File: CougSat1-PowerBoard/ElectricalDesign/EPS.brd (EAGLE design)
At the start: 90.4 x 95.8 mm, 428 parts, among them J1 Deployable 0, J10 Battery -, J11 PGND, J12 Battery +, J13 VBatt, J2 PV0, J3 PV1, J4 Umbilical, J5 CougSat Card, J6 SWD, J7 PV2, J8 PV3, J9 Deployable 1, Q1 CSD25402Q3A, Q10 CSD25402Q3A, Q11 DMN53D0LDW, Q12 CSD25402Q3A, Q13 DMN53D0LDW, Q14 CSD25402Q3A, Q15 DMN53D0LDW, Q16 CSD25402Q3A, Q17 CSD25402Q3A, Q18 CSD25402Q3A, Q19 DMN53D0LDW, Q2 DMN2008LFU, Q20 CSD25402Q3A, Q21 CSD25402Q3A, Q22 CSD25402Q3A, Q23 DMN53D0LDW, Q24 CSD25402Q3A, Q25 DMN53D0LDW, Q26 CSD25402Q3A, Q27 DMN53D0LDW, Q28 CSD25402Q3A, Q29 CSD25402Q3A, Q3 DMN2008LFU, Q30 CSD25402Q3A, Q31 DMN53D0LDW, Q32 CSD25402Q3A, Q33 DMN53D0LDW, Q34 CSD25402Q3A, Q35 CSD25402Q3A, Q36 DMN53D0LDW, Q37 CSD25402Q3A, Q38 CSD25402Q3A, Q39 DMN53D0LDW, Q4 CSD25402Q3A, Q40 CSD25402Q3A, Q41 CSD25402Q3A, Q42 DMN53D0LDW, Q43 CSD25402Q3A, Q5 DMN53D0LDW, Q6 DMN53D0LDW, Q7 CSD25402Q3A, Q8 CSD25402Q3A, Q9 CSD25402Q3A, SW1 ESE24MH1, U1 INA199C2, U10 INA199C2, U11 INA199C1, U12 AD7689, U13 INA199C2, U14 INA199C2, U15 TXS0102DQM, U16 TXS0102DQM, U17 AD8515, U18 BQ29700, U19 INA199C2, U2 AD7689, U20 TXS0102DQM, U21 TXS0102DQM, U22 STM32L476RGT, U23 AD7291, U24 INA199C2, U25 INA199C2, U26 BQ29700, U27 INA199C2, U28 INA199C2, U29 INA199C2, U3 AD8515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

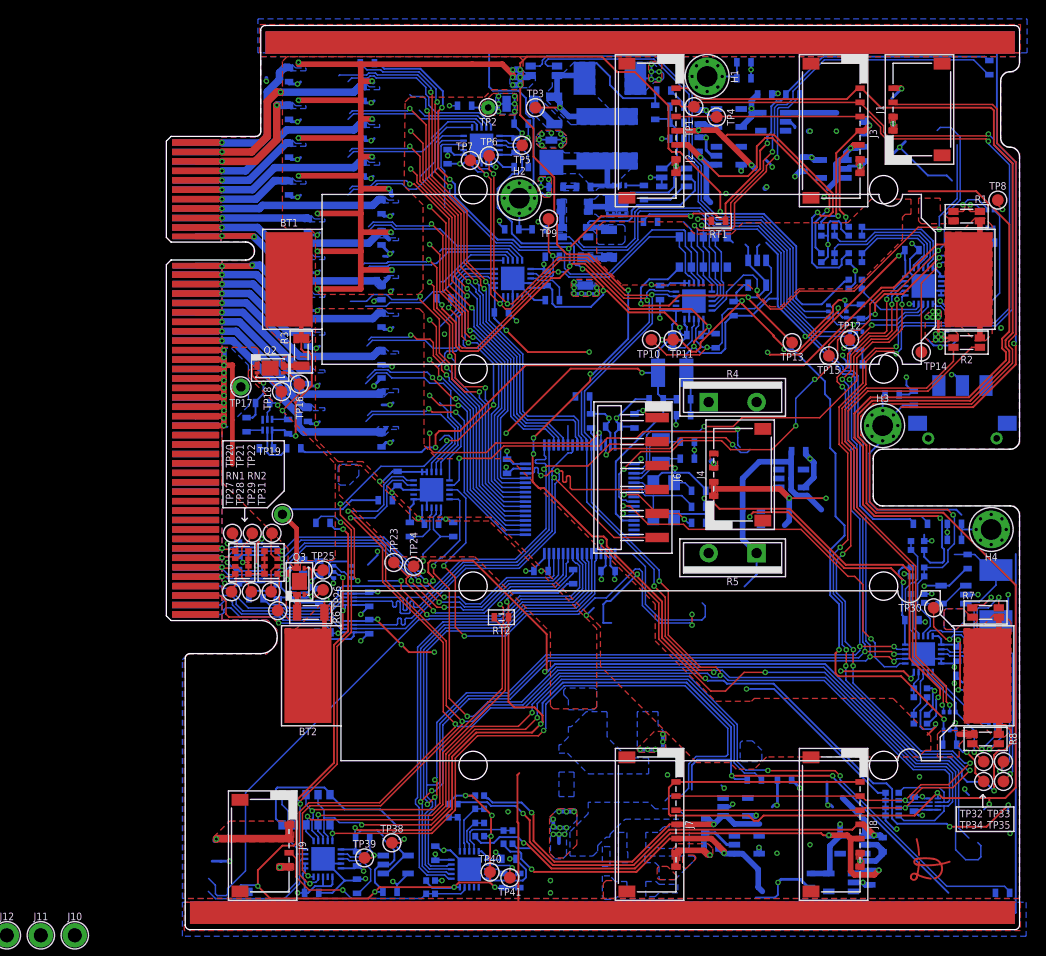
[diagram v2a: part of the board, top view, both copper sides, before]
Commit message: Removed unhelpful copper
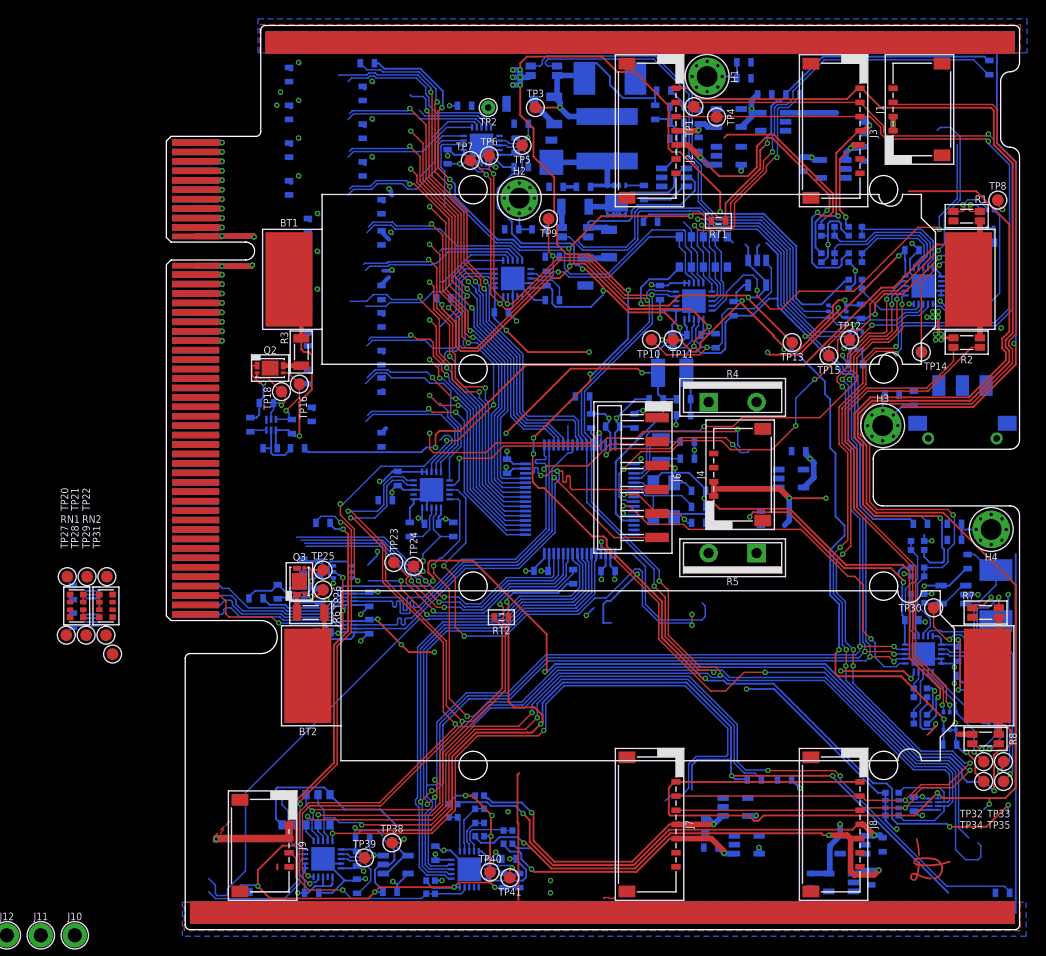
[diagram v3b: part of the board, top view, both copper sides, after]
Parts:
- removed TP17, TP19: TEST_POINT-THT-1.0, CougsInSpace-Connectors:THT-1.0
- moved C51 18.1 mm to (-9.90, -15.1)
- moved C54 18.1 mm to (-9.90, -12.2)
- moved RN1 18.1 mm to (-9.50, -13.6)
- moved RN2 18.1 mm to (-6.40, -13.6)
- moved TP20 18.1 mm to (-10.5, -10.5)
- moved TP21 18.1 mm to (-8.40, -10.5)
- moved TP22 18.1 mm to (-6.30, -10.5)
- moved TP27 18.1 mm to (-10.6, -16.7)
- moved TP28 18.1 mm to (-8.50, -16.7)
- moved TP29 18.1 mm to (-6.40, -16.7)
- moved TP31 18.1 mm to (-5.70, -18.7)
- moved U20 18.1 mm to (-7.80, -15.1)
- moved U21 18.1 mm to (-7.80, -12.2)
- moved C68 0.40 mm to (11.0, 3.10)
- moved C74 0.40 mm to (15.4, 6.70)
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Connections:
- net BATTERY-: no longer TP17.1, TP19.1
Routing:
- net PGND: track 826.7 -> 0.00 mm, vias 122 -> 0
- net 3.3V: track 713.2 -> 592.5 mm, vias 57 -> 55
- net PR_3.3V-0: track 74.9 -> 5.92 mm, vias 3 -> 1
- net CHASSIS: track 252.5 -> 217.8 mm
- net PR_BATT-6: track 28.5 -> 6.27 mm
- net PR_BATT-4: track 26.5 -> 5.85 mm
- net PR_3.3V-1: track 25.9 -> 5.92 mm
- net PR_BATT-2: track 25.4 -> 5.92 mm
- net DGND: track 466.0 -> 447.2 mm, vias 26 -> 24
- net PR_BATT-0: track 24.6 -> 5.92 mm
- net PR_3.3V-9: track 25.0 -> 6.86 mm
- net CHASSIS_RBF1: track 36.2 -> 18.8 mm
- net PR_3.3V-7: track 23.2 -> 5.92 mm
- net PR_3.3V-3: track 22.9 -> 5.92 mm
- net PR_3.3V-5: track 22.0 -> 5.92 mm
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- removed copper zone on layer 1, net 3.3V
- removed copper zone on layer 15, net 3.3V
- removed copper zone on layer 16, net 3.3V
- removed copper zone on layer 2, net 3.3V
- removed copper zone on layer 1, net 3.3V-B
- removed copper zone on layer 15, net 3.3V-B
- removed copper zone on layer 16, net 3.3V-B
- removed copper zone on layer 2, net 3.3V-B
- removed copper zone on layer 16, net 3.3V_I
- removed copper zone on layer 16, net 3.3V_I-B
- removed copper zone on layer 16, net 3.3V_ISENS
- removed copper zone on layer 16, net 3.3V_ISENS-B
- removed copper zone on layer 16, net 3.3V_REG_BUCK_NODE
- removed copper zone on layer 16, net 3.3V_REG_BUCK_NODE-B
- removed copper zone on layer 16, net 3.3V_REG_INCAP
- removed copper zone on layer 16, net 3.3V_REG_INCAP-B
- removed copper zone on layer 16, net 3.3V_REG_OUTCAP
- removed copper zone on layer 16, net 3.3V_REG_OUTCAP-B
- removed copper zone on layer 16, net 3.3V_REG_RSENS
- removed copper zone on layer 16, net 3.3V_REG_RSENS-B
- removed copper zone on layer 16, net 3.3V_REG_SNUBBER
- removed copper zone on layer 16, net 3.3V_REG_SNUBBER-B
- removed copper zone on layer 2, net AGND
- removed copper zone on layer 15, net AVDD
- removed copper zone on layer 15, net BALANCING-2
- removed copper zone on layer 2, net BALANCING-2
- removed copper zone on layer 1, net BALANCING-TOP
- removed copper zone on layer 16, net BALANCING-TOP
- removed copper zone on layer 1, net BP_VSS-A
- removed copper zone on layer 1, net BP_VSS-A1
- removed copper zone on layer 1, net BP_VSS_I-A
- removed copper zone on layer 1, net BP_VSS_I-B
- removed copper zone on layer 15, net CHASSIS
- removed copper zone on layer 2, net CHASSIS
- removed copper zone on layer 2, net DGND
- removed copper zone on layer 16, net PGND
- removed copper zone on layer 2, net PGND
- removed copper zone on layer 16, net PR_3.3V-0
- removed copper zone on layer 16, net PR_3.3V-1
- removed copper zone on layer 16, net PR_3.3V-10
- removed copper zone on layer 16, net PR_3.3V-11
- removed copper zone on layer 16, net PR_3.3V-12
- removed copper zone on layer 16, net PR_3.3V-2
- removed copper zone on layer 16, net PR_3.3V-3
- removed copper zone on layer 16, net PR_3.3V-4
- removed copper zone on layer 16, net PR_3.3V-5
- removed copper zone on layer 16, net PR_3.3V-6
- removed copper zone on layer 16, net PR_3.3V-7
- removed copper zone on layer 16, net PR_3.3V-8
- removed copper zone on layer 16, net PR_3.3V-9
- removed copper zone on layer 16, net PR_BATT-0
- removed copper zone on layer 16, net PR_BATT-1
- removed copper zone on layer 16, net PR_BATT-2
- removed copper zone on layer 16, net PR_BATT-3
- removed copper zone on layer 16, net PR_BATT-4
- removed copper zone on layer 16, net PR_BATT-5
- removed copper zone on layer 16, net PR_BATT-6
- removed copper zone on layer 1, net PR_DP-0
- removed copper zone on layer 1, net UMB_IN
- removed copper zone on layer 1, net VBATT-A
- removed copper zone on layer 15, net VBATT-A
- removed copper zone on layer 16, net VBATT-A
- removed copper zone on layer 1, net VBATT-B
- removed copper zone on layer 15, net VBATT-B
- removed copper zone on layer 16, net VBATT-B
- removed copper zone on layer 2, net VBATT-B
- removed copper zone on layer 1, net VIN
- removed copper zone on layer 15, net VIN
- removed copper zone on layer 16, net VIN
- removed copper zone on layer 2, net VIN
- removed copper zone on layer 1, net VIN-B
- removed copper zone on layer 15, net VIN-B
- removed copper zone on layer 16, net VIN-B
- removed copper zone on layer 2, net VIN-B
- removed copper zone on layer 1, net VIN_OUT-A
- removed copper zone on layer 1, net VIN_OUT-B
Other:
- board text removed: "A"
- board text removed: "B"

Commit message: Laid out output switching
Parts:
- moved R12 240.6 mm to (37.7, 17.2), flipped to the bottom, turned to 270 degrees
- moved R38 236.9 mm to (32.7, 15.6), flipped to the bottom, turned to 90 degrees
- moved R45 235.1 mm to (37.7, 13.1), flipped to the bottom, turned to 270 degrees
- moved R51 231.6 mm to (32.7, 11.5), flipped to the bottom, turned to 90 degrees
- moved R55 229.6 mm to (37.7, 9.00), flipped to the bottom, turned to 270 degrees
- moved R73 226.3 mm to (32.7, 7.40), flipped to the bottom, turned to 90 degrees
- moved R26 224.3 mm to (24.8, 13.9), flipped to the bottom, turned to 180 degrees
- moved R76 224.3 mm to (37.7, 4.90), flipped to the bottom, turned to 270 degrees
- moved R39 222.6 mm to (29.5, 12.1), flipped to the bottom, turned to 180 degrees
- moved R10 218.1 mm to (29.5, 16.2), flipped to the bottom, turned to 180 degrees
- moved R50 218.1 mm to (24.8, 9.80), flipped to the bottom, turned to 180 degrees
- moved Q25 216.4 mm to (35.2, 10.4), flipped to the bottom
- moved R54 216.3 mm to (29.5, 8.00), flipped to the bottom, turned to 180 degrees
- moved R56 212.2 mm to (24.8, 5.70), flipped to the bottom, turned to 180 degrees
- moved Q33 211.5 mm to (35.2, 6.30), flipped to the bottom
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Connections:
- net !PC_BATT-0: now also Q31.3; no longer Q13.6
- net !PC_BATT-1: now also Q13.6; no longer Q13.3
- net !PC_BATT-2: now also Q13.3; no longer Q25.6
- net !PC_BATT-3: now also Q25.6; no longer Q25.3
- net !PC_BATT-4: now also Q25.3; no longer Q33.6
- net !PC_BATT-5: now also Q33.6; no longer Q33.3
- net !PC_BATT-6: now also Q33.3; no longer Q36.6
- net !PC_BH-0: now also Q36.6; no longer Q36.3
- net PC_BATT-0: now also Q31.5; no longer Q13.2
- net PC_BATT-1: now also Q13.2; no longer Q13.5
- net PC_BATT-2: now also Q13.5; no longer Q25.2
- net PC_BATT-3: now also Q25.2; no longer Q25.5
- net PC_BATT-4: now also Q25.5; no longer Q33.2
- net PC_BATT-5: now also Q33.2; no longer Q33.5
- net PC_BATT-6: now also Q33.5; no longer Q36.2
- net PC_BH-0: now also Q36.2; no longer Q36.5
- net PGND: now also Q31.4; no longer Q36.4
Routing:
- net AGND: track 630.6 -> 0.00 mm, vias 43 -> 0
- net 3.3V: track 592.5 -> 105.3 mm, vias 55 -> 13
- net DGND: track 447.2 -> 0.00 mm, vias 24 -> 0
- net AVDD: track 341.0 -> 0.00 mm, vias 22 -> 0
- net I2C_SCL: track 228.3 -> 0.00 mm, vias 8 -> 0
- net I2C_SDA: track 227.8 -> 0.00 mm, vias 8 -> 0
- net CHASSIS: track 217.8 -> 0.00 mm, vias 1 -> 0
- net PR_3.3V-PV: track 196.9 -> 0.00 mm, vias 2 -> 0
- net VBATT-A: track 167.3 -> 0.00 mm, vias 2 -> 0
- net PV_I2C_SDA: track 163.4 -> 0.00 mm, vias 7 -> 0
- net PV_I2C_SCL: track 162.2 -> 0.00 mm, vias 7 -> 0
- net SPI_MISO: track 157.5 -> 0.00 mm, vias 7 -> 0
- net SPI_MOSI: track 156.0 -> 0.00 mm, vias 6 -> 0
- net SPI_SCK: track 154.9 -> 0.00 mm, vias 4 -> 0
- net VIN: track 145.3 -> 0.00 mm, vias 17 -> 0
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- added copper zone on layer 16, net PR_FET_3.3V-0
- added copper zone on layer 16, net PR_FET_3.3V-1
- added copper zone on layer 16, net PR_FET_3.3V-10
- added copper zone on layer 16, net PR_FET_3.3V-11
- added copper zone on layer 16, net PR_FET_3.3V-12
- added copper zone on layer 16, net PR_FET_3.3V-2
- added copper zone on layer 16, net PR_FET_3.3V-3
- added copper zone on layer 16, net PR_FET_3.3V-4
- added copper zone on layer 16, net PR_FET_3.3V-5
- added copper zone on layer 16, net PR_FET_3.3V-6
- added copper zone on layer 16, net PR_FET_3.3V-7
- added copper zone on layer 16, net PR_FET_3.3V-8
- added copper zone on layer 16, net PR_FET_3.3V-9
- added copper zone on layer 16, net PR_FET_BATT-0
- added copper zone on layer 16, net PR_FET_BATT-1
- added copper zone on layer 16, net PR_FET_BATT-2
- added copper zone on layer 16, net PR_FET_BATT-3
- added copper zone on layer 16, net PR_FET_BATT-4
- added copper zone on layer 16, net PR_FET_BATT-5
- added copper zone on layer 16, net PR_FET_BATT-6

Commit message: Began output current sensing layout
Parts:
- removed TP36, TP37, TP42, TP43, TP44, TP45, TP46, TP47, TP48, TP49, TP50, TP51, TP52, TP53, TP54, TP55, TP56, TP57, TP58, TP59, TP60, TP61, TP62, TP63, TP64: TEST_POINT-SMD-C-1.25, CougsInSpace-Connectors:SMD-C-1.25
- moved U25 225.0 mm to (47.9, 10.9), flipped to the bottom
- moved U4 225.0 mm to (47.9, 20.5), flipped to the bottom
- moved U19 220.5 mm to (47.9, 17.7), flipped to the bottom
- moved U7 220.5 mm to (44.6, 17.7), flipped to the bottom
- moved U28 220.1 mm to (47.9, 8.10), flipped to the bottom
- moved U27 220.1 mm to (44.6, 8.10), flipped to the bottom
- moved U24 212.3 mm to (44.6, 10.9), flipped to the bottom
- moved U42 121.7 mm to (44.8, 34.8)
- moved U45 121.0 mm to (47.9, 26.1)
- moved U46 120.9 mm to (44.6, 23.3)
- moved U36 120.7 mm to (40.8, 37.6)
- moved U41 115.2 mm to (41.5, 34.8)
- moved U48 111.4 mm to (47.9, 23.3)
- moved U38 110.5 mm to (44.1, 37.6)
- moved U43 109.3 mm to (44.6, 26.1)
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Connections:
- net BP_VSS-A1 renamed BP_VSS-B
- net AGND: no longer RT10.1, U1.1, U1.2, U14.1, U14.2, U19.1, U19.2, U24.1, U24.2, U25.1, U25.2, U27.1, U27.2, U28.1, U28.2, U29.1, U29.2, U30.1, U30.2, U32.1, U32.2, U33.1, U33.2, U36.1, U36.2, U38.1, U38.2, U4.1, U4.2, U41.1, U41.2, U42.1, U42.2, U43.1, U43.2, U45.1, U45.2, U46.1, U46.2, U48.1, U48.2, U49.1, U49.2, U51.1, U51.2, U6.1, U6.2, U7.1, U7.2, U9.1, U9.2
- net I_3.3V-0: no longer TP37.1
- net I_3.3V-1: no longer TP36.1
- net I_3.3V-10: no longer TP50.1
- net I_3.3V-11: no longer TP51.1
- net I_3.3V-12: no longer TP52.1
- net I_3.3V-2: no longer TP42.1
- net I_3.3V-3: no longer TP43.1
- net I_3.3V-4: no longer TP44.1
- net I_3.3V-5: no longer TP45.1
- net I_3.3V-6: no longer TP46.1
- net I_3.3V-7: no longer TP47.1
- net I_3.3V-8: no longer TP48.1
- net I_3.3V-9: no longer TP49.1
- net I_3.3V-PV: no longer TP64.1
- net I_BATT-0: no longer TP53.1
- net I_BATT-1: no longer TP54.1
- net I_BATT-2: no longer TP55.1
- net I_BATT-3: no longer TP56.1
- net I_BATT-4: no longer TP57.1
- net I_BATT-5: no longer TP58.1
- net I_BATT-6: no longer TP59.1
- net I_BH-0: no longer TP60.1
- net I_BH-1: no longer TP61.1
- net I_DP-0: no longer TP62.1
- net I_DP-1: no longer TP63.1
- net PGND: now also RT10.1, U1.1, U1.2, U14.1, U14.2, U19.1, U19.2, U24.1, U24.2, U25.1, U25.2, U27.1, U27.2, U28.1, U28.2, U29.1, U29.2, U30.1, U30.2, U32.1, U32.2, U33.1, U33.2, U36.1, U36.2, U38.1, U38.2, U4.1, U4.2, U41.1, U41.2, U42.1, U42.2, U43.1, U43.2, U45.1, U45.2, U46.1, U46.2, U48.1, U48.2, U49.1, U49.2, U51.1, U51.2, U6.1, U6.2, U7.1, U7.2, U9.1, U9.2
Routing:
- net PGND: track 93.0 -> 235.4 mm, vias 15 -> 33
- net BP_VSS-A: track 0.00 -> 29.9 mm, vias 0 -> 1
- net JTAG_EN_PMIC: track 0.00 -> 28.0 mm, vias 0 -> 4
- net AVDD: track 0.00 -> 25.1 mm, vias 0 -> 7
- net I_3.3V-6_N: track 0.00 -> 21.8 mm, vias 0 -> 2
- net I_3.3V-7_N: track 0.00 -> 21.1 mm, vias 0 -> 2
- net I_3.3V-6_P: track 0.00 -> 21.1 mm, vias 0 -> 2
- net I_3.3V-7_P: track 0.00 -> 19.8 mm, vias 0 -> 2
- net I_3.3V-4_N: track 0.00 -> 19.7 mm, vias 0 -> 2
- net I_3.3V-2_N: track 0.00 -> 19.2 mm, vias 0 -> 2
- net BATTERY-: track 0.00 -> 19.1 mm, vias 0 -> 2
- net I_3.3V-5_N: track 0.00 -> 19.1 mm, vias 0 -> 2
- net I_3.3V-0_N: track 0.00 -> 18.7 mm, vias 0 -> 2
- net I_3.3V-3_N: track 0.00 -> 18.6 mm, vias 0 -> 2
- net I_3.3V-4_P: track 0.00 -> 18.4 mm, vias 0 -> 2
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- added copper zone on layer 1, net BATTERY-
- added copper zone on layer 1, net BP_VSS-A
- added copper zone on layer 1, net BP_VSS-B
- added copper zone on layer 1, net BP_VSS_I-A
- added copper zone on layer 1, net BP_VSS_I-B
- added copper zone on layer 16, net PR_3.3V-0
- added copper zone on layer 16, net PR_3.3V-1
- added copper zone on layer 16, net PR_3.3V-10
- added copper zone on layer 16, net PR_3.3V-11
- added copper zone on layer 16, net PR_3.3V-12
- added copper zone on layer 16, net PR_3.3V-2
- added copper zone on layer 16, net PR_3.3V-3
- added copper zone on layer 16, net PR_3.3V-4
- added copper zone on layer 16, net PR_3.3V-5
- added copper zone on layer 16, net PR_3.3V-6
- added copper zone on layer 16, net PR_3.3V-7
- added copper zone on layer 16, net PR_3.3V-8
- added copper zone on layer 16, net PR_3.3V-9
- added copper zone on layer 16, net PR_BATT-0
- added copper zone on layer 16, net PR_BATT-1
- added copper zone on layer 16, net PR_BATT-2
- added copper zone on layer 16, net PR_BATT-3
- added copper zone on layer 16, net PR_BATT-4
- added copper zone on layer 16, net PR_BATT-5
- added copper zone on layer 16, net PR_BATT-6
- removed copper zone on layer 1, net PGND
- removed copper zone on layer 1, net PR_DP-1

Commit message: Laid out output current sensing
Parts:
- moved DS3 304.8 mm to (191.5, -13.8)
- moved Q37 304.8 mm to (196.1, 16.2)
- moved Q38 304.8 mm to (200.6, 16.2)
- moved Q40 304.8 mm to (205.1, 16.2)
- moved Q41 304.8 mm to (209.6, 16.2)
- moved Q43 304.8 mm to (214.1, 16.2)
- moved R81 304.8 mm to (214.4, -7.30)
- moved R84 304.8 mm to (196.4, -0.50)
- moved R85 304.8 mm to (217.3, -7.30)
- moved R86 304.8 mm to (201.1, -0.50)
- moved R87 304.8 mm to (190.8, -10.6)
- moved R88 304.8 mm to (205.8, -0.50)
- moved R90 304.8 mm to (210.5, -0.50)
- moved R91 304.8 mm to (196.6, -10.6)
- moved RN22 304.8 mm to (193.1, -18.6)
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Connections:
- net AGND: now also U23.5; no longer U23.4
- net I_3.3V-PV: now also U23.4; no longer U23.5
- net I_BATT-3: now also U23.3; no longer U23.1
- net I_BATT-4: now also U23.2; no longer U23.20
- net I_BATT-5: now also U23.1; no longer U23.19
- net I_BATT-6: now also U23.20; no longer U23.18
- net I_BH-0: no longer U23.2
- net I_BH-1: no longer U23.3
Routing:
- net PGND: track 235.4 -> 304.4 mm, vias 33 -> 47
- net AVDD: track 25.1 -> 87.9 mm, vias 7 -> 21
- net I2C_SDA: track 0.00 -> 31.9 mm, vias 0 -> 3
- net I2C_SCL: track 0.00 -> 31.6 mm, vias 0 -> 3
- net DGND: track 13.4 -> 41.9 mm, vias 3 -> 5
- net I_BATT-5_N: track 1.04 -> 25.2 mm, vias 1 -> 2
- net I_BATT-3_N: track 1.04 -> 24.4 mm, vias 1 -> 2
- net I_BATT-6_N: track 1.04 -> 24.0 mm, vias 1 -> 2
- net I_BATT-1_N: track 1.04 -> 23.8 mm, vias 1 -> 2
- net I_BATT-4_N: track 1.04 -> 23.7 mm, vias 1 -> 2
- net I_BATT-5_P: track 1.04 -> 23.6 mm, vias 1 -> 2
- net I_3.3V-12_N: track 1.04 -> 23.3 mm, vias 1 -> 2
- net I_BATT-2_N: track 1.04 -> 23.1 mm, vias 1 -> 2
- net I_BATT-3_P: track 1.04 -> 23.1 mm, vias 1 -> 2
- net I_BATT-6_P: track 1.04 -> 22.9 mm, vias 1 -> 2
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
